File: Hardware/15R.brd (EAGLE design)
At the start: 360.5 x 217.5 mm, 667 parts, among them J2 USB Female Type C Connector, J3 AUDIO_JACK_TRRSSMD_RA, Q2 MBT3904DW1T1, U2 ESP-WROOM-32NARROW, U3 AP2112K-3.3V, U4 CP2102N, U5 ADMP401

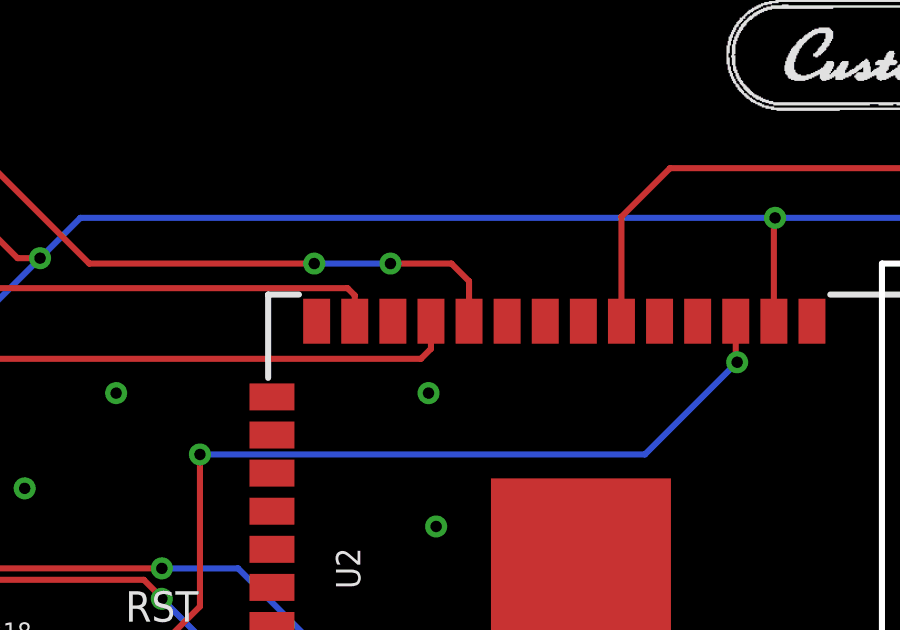
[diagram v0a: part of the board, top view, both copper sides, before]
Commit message: adding in left/right for mic capability
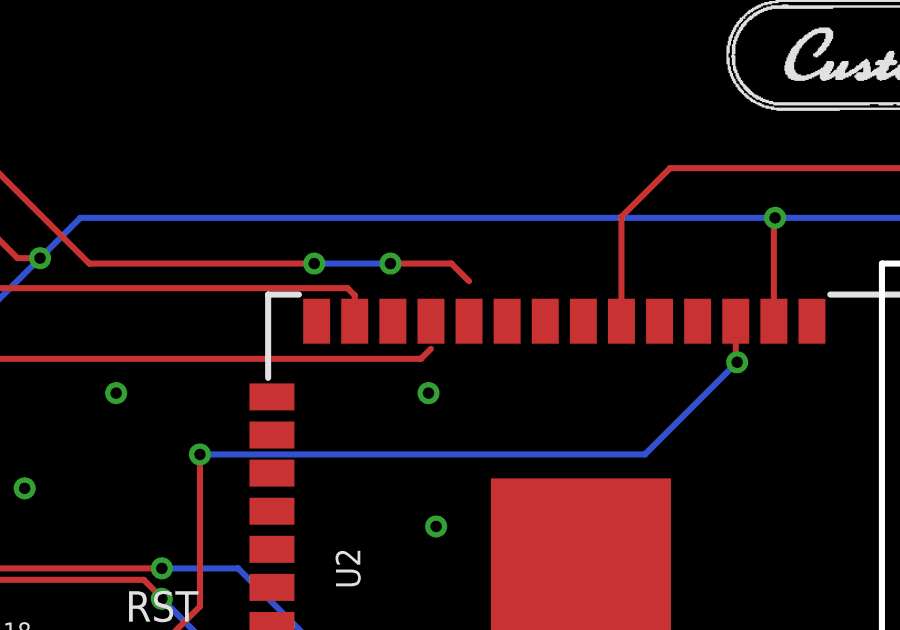
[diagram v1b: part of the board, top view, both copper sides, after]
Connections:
- removed net 32: U2.8
- removed net 33: U2.9
- net RING1: now also U2.9; no longer U2.11
- net TIP: now also U2.8; no longer U2.10
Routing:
- net TIP: track 48.1 -> 46.7 mm
- net RING1: track 45.2 -> 44.3 mm
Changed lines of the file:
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@@
 <?xml version="1.0" encoding="utf-8"?>
 <!DOCTYPE eagle SYSTEM "eagle.dtd">
-<eagle version="9.3.1">
+<eagle version="9.1.0">
 <drawing>
 <settings>
@@
 <contactref element="U2" pad="36"/>
 </signal>
-<signal name="32">
-<contactref element="U2" pad="8"/>
-</signal>
 <signal name="15">
 <contactref element="U2" pad="23"/>
 </signal>
-<signal name="33">
-<contactref element="U2" pad="9"/>
-</signal>
 <signal name="27">
 <contactref element="U2" pad="12"/>
@@
 <contactref element="R7" pad="1"/>
 <contactref element="R6" pad="2"/>
-<contactref element="U2" pad="11"/>
 <wire x1="8.61" y1="31.63" x2="8.61" y2="29.725" width="0.2032" layer="1"/>
 <wire x1="8.61" y1="27.82" x2="8.61" y2="29.725" width="0.2032" layer="1"/>
@@
 <wire x1="8.61" y1="27.82" x2="17.36" y2="27.82" width="0.2032" layer="1"/>
 <wire x1="44.196" y1="17.145" x2="44.53" y2="17.479" width="0.2032" layer="1"/>
-<wire x1="44.53" y1="17.479" x2="44.53" y2="18.398" width="0.2032" layer="1"/>
 <wire x1="28.035" y1="17.145" x2="44.196" y2="17.145" width="0.2032" layer="1"/>
+<contactref element="U2" pad="9"/>
+<wire x1="44.53" y1="17.479" x2="47.07" y2="18.398" width="0" layer="19" extent="1-1"/>
 </signal>
 <signal name="TIP">
@@
 <contactref element="R12" pad="2"/>
 <contactref element="C3" pad="1"/>
-<contactref element="U2" pad="10"/>
 <wire x1="8.61" y1="37.345" x2="8.61" y2="35.44" width="0.2032" layer="1"/>
 <wire x1="8.61" y1="33.535" x2="8.61" y2="35.44" width="0.2032" layer="1"/>
-<wire x1="45.8" y1="18.398" x2="45.8" y2="19.732" width="0.2032" layer="1"/>
 <wire x1="45.212" y1="20.32" x2="45.8" y2="19.732" width="0.2032" layer="1"/>
 <wire x1="45.212" y1="20.32" x2="43.18" y2="20.32" width="0.2032" layer="1"/>
@@
 <wire x1="33.14" y1="20.32" x2="19.925" y2="33.535" width="0.2032" layer="1"/>
 <wire x1="19.925" y1="33.535" x2="8.61" y2="33.535" width="0.2032" layer="1"/>
+<contactref element="U2" pad="8"/>
+<wire x1="45.8" y1="19.732" x2="48.34" y2="18.398" width="0" layer="19" extent="1-1"/>
 </signal>
 <signal name="DIO0">

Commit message: starting to reroute 15 inch model
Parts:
- moved J3 369.0 mm to (360.2, 28.6), turned to 180 degrees
- moved J2 356.4 mm to (353.3, 47.4), turned to 90 degrees
- moved R3 350.3 mm to (350.1, 48.8), turned to 0 degrees
- moved R4 349.9 mm to (350.1, 46.3), turned to 0 degrees
- moved R15 341.2 mm to (346.3, 26.1), turned to 270 degrees
- moved R14 341.1 mm to (346.3, 31.8), turned to 270 degrees
- moved R12 336.2 mm to (343.7, 24.2), turned to 180 degrees
- moved C3 336.1 mm to (343.7, 26.1), turned to 0 degrees
- moved R6 336.0 mm to (343.7, 33.7), turned to 180 degrees
- moved R5 336.0 mm to (343.7, 28.0), turned to 180 degrees
- moved C2 336.0 mm to (343.7, 31.8), turned to 180 degrees
- moved R7 336.0 mm to (343.7, 29.9), turned to 0 degrees
- moved C9 62.4 mm to (10.9, 17.7), turned to 90 degrees
- moved D299 60.2 mm to (142.3, 52.5)
- moved JP299 60.2 mm to (142.3, 52.5)
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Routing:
- net N$139: track 0.00 -> 350.3 mm, vias 0 -> 2
- net N$140: track 0.00 -> 350.1 mm, vias 0 -> 2
- net N$144: track 0.00 -> 349.1 mm, vias 0 -> 2
- net N$147: track 0.00 -> 348.2 mm, vias 0 -> 2
- net N$68: track 0.00 -> 347.8 mm, vias 0 -> 2
- net DIO152: track 0.00 -> 333.3 mm, vias 0 -> 2
- net 3.3V: track 167.3 -> 32.7 mm, vias 10 -> 4
- net V_USB: track 428.6 -> 511.4 mm, vias 266 -> 314
- net DIO0: track 249.7 -> 184.1 mm, vias 3 -> 1
- net TIP: track 46.7 -> 3.81 mm, vias 2 -> 0
- net RING1: track 44.3 -> 3.81 mm
- net MIC: track 32.4 -> 5.10 mm
- net D-: track 31.8 -> 9.11 mm
- net D+: track 31.5 -> 8.97 mm
- net N$148: track 0.00 -> 17.5 mm
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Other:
- outline, holes or cut-outs redrawn
- board text removed: "5V"
- board text removed: "D"

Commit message: routing 15 inch
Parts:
- R13: value 1k -> 2.2k; device SparkFun-Resistors:AXIAL-0.3 -> SparkFun-Resistors:0603
- moved R13 9.70 mm to (16.5, 12.0), turned to 180 degrees
- moved C7 8.98 mm to (7.97, 21.6), turned to 0 degrees
- moved R9 7.80 mm to (25.0, 17.7)
- moved C1 6.47 mm to (7.97, 19.8), turned to 0 degrees
- moved C8 5.59 mm to (5.00, 16.5), turned to 90 degrees
- moved R8 3.81 mm to (7.75, 12.8), turned to 180 degrees
- moved U$2 2.50 mm to (16.5, 17.7)
- moved C9 2.50 mm to (13.4, 17.7)
- moved U3 2.18 mm to (7.97, 16.6), turned to 0 degrees
- moved R11 1.96 mm to (16.5, 13.5)
- moved C5 1.66 mm to (16.5, 15.0)
- moved C4 1.13 mm to (20.0, 15.0), turned to 180 degrees
- moved C6 1.00 mm to (20.1, 17.7)
- moved R10 1.00 mm to (22.0, 17.7)
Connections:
- net N$11: now also R13.1; no longer R13.P$1
- net N$9: now also R13.2; no longer R13.P$2
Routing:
- net 3.3V: track 32.7 -> 435.0 mm, vias 4 -> 9
- net D-: track 9.11 -> 384.3 mm
- net D+: track 8.97 -> 382.6 mm
- net RING1: track 3.81 -> 316.9 mm
- net TIP: track 3.81 -> 314.1 mm
- net DIO0: track 184.1 -> 231.6 mm, vias 1 -> 2
- net MIC: track 5.10 -> 29.4 mm
- net V_USB: track 511.4 -> 523.0 mm, vias 314 -> 315
- net TX: track 23.6 -> 34.5 mm, vias 1 -> 2
- net RX: track 23.5 -> 33.6 mm, vias 1 -> 2
- net N$9: track 8.10 -> 13.4 mm
- net RTS: track 11.3 -> 9.42 mm
- net N$16: track 5.73 -> 7.24 mm
- net GND: track 3.83 -> 5.09 mm, vias 13 -> 19
- net N$11: track 4.84 -> 3.83 mm
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
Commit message: updating 13 inch, finish layout of 15 inch
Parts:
- removed D249: WS2812B, SparkFun-LED:WS2812B
- removed FRAME1, FRAME2, FRAME3, FRAME4: FRAME-LEDGER, SparkFun-Aesthetics:CREATIVE_COMMONS
- removed JP249: JUMPER-SMT_2_NO_NO-SILK, SparkFun-Jumpers:SMT-JUMPER_2_NO_NO-SILK
- added D309, D310, D311, D315: WS2812B, SparkFun-LED:WS2812B
- added JP309, JP310, JP311, JP315: JUMPER-SMT_2_NO_NO-SILK, SparkFun-Jumpers:SMT-JUMPER_2_NO_NO-SILK
- moved D248 80.8 mm to (7.50, 37.5)
- moved JP248 80.8 mm to (7.50, 37.5)
- moved D250 45.0 mm to (67.5, 7.50)
- moved D251 45.0 mm to (82.5, 7.50)
- moved D252 45.0 mm to (97.5, 7.50)
- moved D253 45.0 mm to (112.5, 7.50)
- moved D254 45.0 mm to (127.5, 7.50)
- moved D255 45.0 mm to (143.8, 7.50)
- moved D256 45.0 mm to (157.5, 7.50)
- moved D257 45.0 mm to (172.5, 7.50)
- moved JP250 45.0 mm to (67.5, 7.50)
- moved JP251 45.0 mm to (82.5, 7.50)
- moved JP252 45.0 mm to (97.5, 7.50)
- moved JP253 45.0 mm to (112.5, 7.50)
- moved JP254 45.0 mm to (127.5, 7.50)
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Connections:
- removed net DIO120: D231.2, D232.4, JP231.2, JP232.1
- removed net DIO131: D248.2, D249.4, JP248.2, JP249.1
- new net DIO143: D309.2, D310.4, JP309.2, JP310.1
- new net DIO153: D232.4, D315.2, JP232.1, JP315.2
- new net N$170: D310.2, D311.4, JP310.2, JP311.1
- new net N$172: D231.2, D309.4, JP231.2, JP309.1
- new net N$173: D311.2, D315.4, JP311.2, JP315.1
- net DIO152: now also D248.4, JP248.1; no longer D212.4, JP212.1
- net GND: now also D309.3, D310.3, D311.3, D315.3; no longer D249.3
- net N$125: now also D212.4, D248.2, JP212.1, JP248.2; no longer D247.2, D248.4, JP247.2, JP248.1
- net N$128: now also D247.2, JP247.2; no longer D249.2, JP249.2
- net V_USB: now also D309.1, D310.1, D311.1, D315.1; no longer D249.1
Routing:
- net N$172: track 0.00 -> 348.9 mm, vias 0 -> 2
- net N$128: track 16.8 -> 294.2 mm, vias 0 -> 2
- net DIO120: track 273.9 -> 0.00 mm, vias 2 -> 0
- net N$125: track 274.1 -> 17.2 mm
- net N$170: track 0.00 -> 46.8 mm, vias 0 -> 2
- net DIO136: track 16.8 -> 63.6 mm
- net V_USB: track 523.0 -> 550.9 mm, vias 315 -> 317
- net DIO143: track 0.00 -> 17.5 mm, vias 0 -> 2
- net DIO153: track 0.00 -> 16.9 mm
- net N$173: track 0.00 -> 16.8 mm
- net DIO131: track 16.8 -> 0.00 mm
- net DIO152: track 333.3 -> 348.3 mm
- net D+: track 382.6 -> 377.7 mm
- net D-: track 384.3 -> 379.6 mm
- net N$129: track 21.3 -> 18.1 mm
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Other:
- board text added: "15R"
- board text removed: "13R"
